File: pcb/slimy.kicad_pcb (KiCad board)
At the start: 2 copper layers, 266.7 x 95.3 mm, 100 parts, among them K1 KEYSW, K10 KEYSW, K11 KEYSW, K12 KEYSW, K13 KEYSW, K14 KEYSW, K15 KEYSW, K16 KEYSW, K17 KEYSW, K18 KEYSW, K19 KEYSW, K2 KEYSW, K20 KEYSW, K21 KEYSW, K22 KEYSW, K23 KEYSW, K24 KEYSW, K25 KEYSW, K26 KEYSW, K27 KEYSW, K28 KEYSW, K29 KEYSW, K3 KEYSW, K30 KEYSW, K31 KEYSW, K32 KEYSW, K33 KEYSW, K34 KEYSW, K35 KEYSW, K36 KEYSW, K37 KEYSW, K38 KEYSW, K39 KEYSW, K4 KEYSW, K40 KEYSW, K41 KEYSW, K42 KEYSW, K43 KEYSW, K44 KEYSW, K45 KEYSW, K46 KEYSW, K47 KEYSW, K48 KEYSW, K5 KEYSW, K6 KEYSW, K7 KEYSW, K8 KEYSW, K9 KEYSW, U1 Teensy3.2, U2 ST7789_SPI, U3 PIM447

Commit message: Thicker logo lines
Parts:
- moved G*** 0.28 mm to (215.6, 144.1)

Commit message: Add keyboard name
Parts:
- added G***: LOGO, slimy_footprints:text, B.Cu at (215.7, 175.5)
- added kibuzzard-62A5BC49: G***, kibuzzard-62A5BC49, B.Cu at (208.9, 176.7)

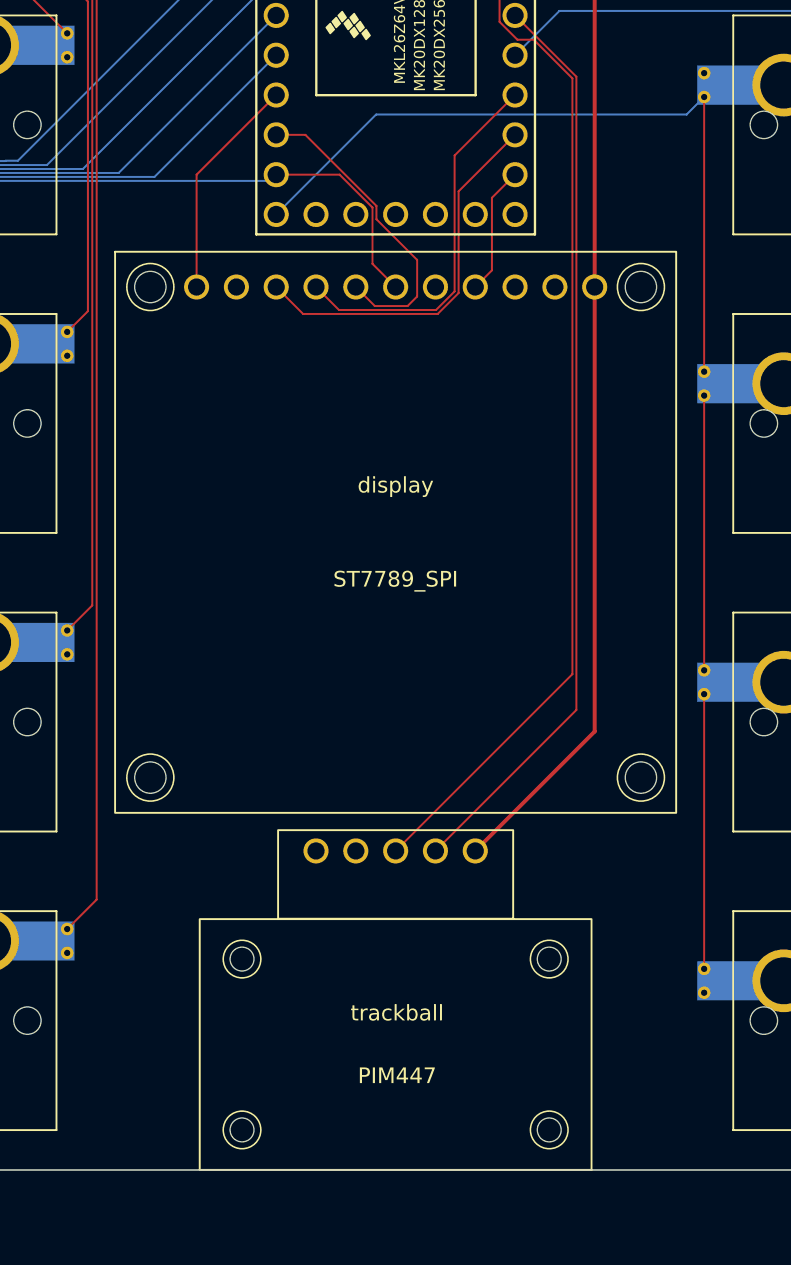
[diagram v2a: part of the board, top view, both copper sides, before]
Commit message: Fix screen and trackball footprints
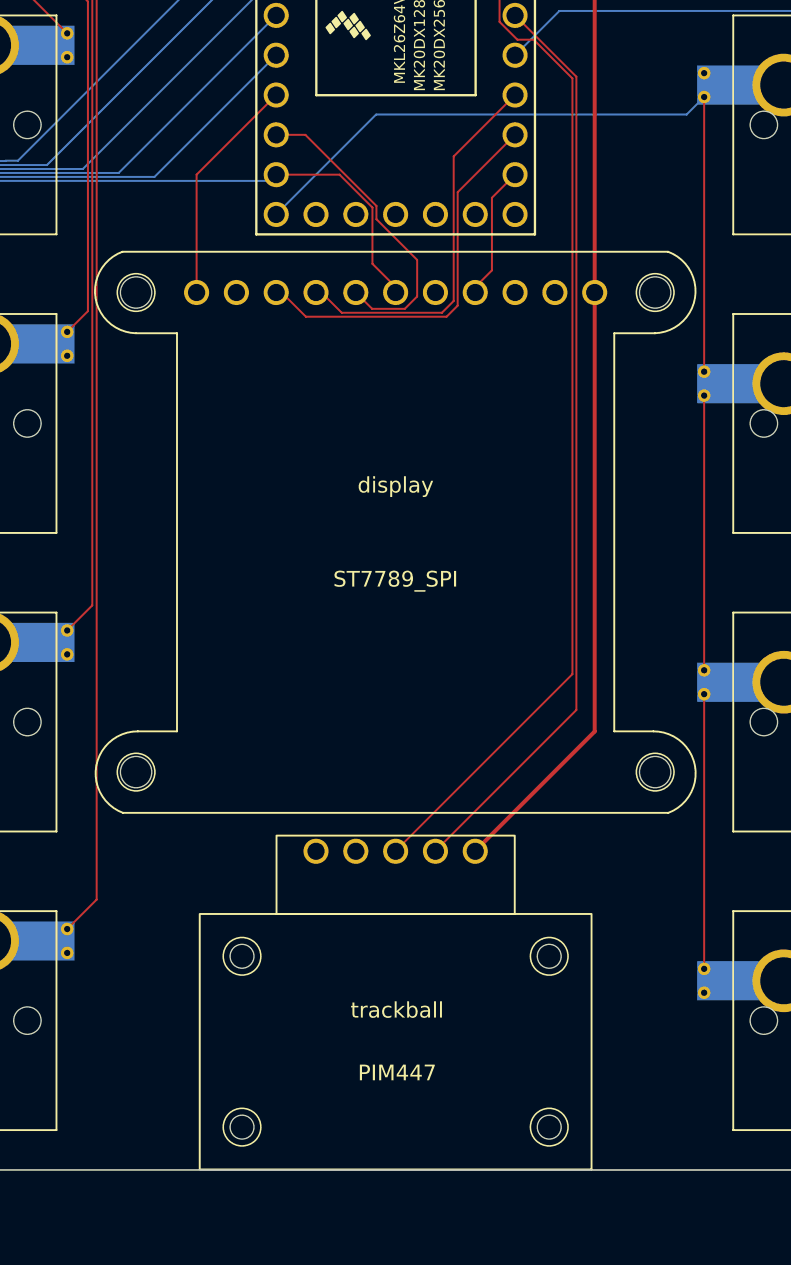
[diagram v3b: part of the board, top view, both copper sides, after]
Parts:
- moved U3 0.18 mm to (215.7, 175.4)
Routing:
- net LCD DC: track 24.5 -> 25.1 mm

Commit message: Fix keycap overlap with display
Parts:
- moved D25 0.26 mm to (246.0, 104.3)
- moved D26 0.26 mm to (243.0, 100.0)
- moved D29 0.26 mm to (265.1, 104.3)
- moved D30 0.26 mm to (262.1, 100.0)
- moved D31 0.26 mm to (259.0, 95.7)
- moved D32 0.26 mm to (256.0, 91.3)
- moved D33 0.26 mm to (284.1, 104.3)
- moved D34 0.26 mm to (281.1, 100.0)
- moved D35 0.26 mm to (278.1, 95.7)
- moved D36 0.26 mm to (275.0, 91.3)
- moved D41 0.26 mm to (322.2, 104.3)
- moved D42 0.26 mm to (319.2, 100.0)
- moved D43 0.26 mm to (316.2, 95.7)
- moved D44 0.26 mm to (313.1, 91.3)
- moved D45 0.26 mm to (341.3, 104.3)
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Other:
- board size 266.7 x 95.3 mm -> 267.2 x 95.3 mm
